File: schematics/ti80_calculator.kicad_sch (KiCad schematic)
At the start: 117 parts, among them J10 0, J13 0, J14 0Ω, J15 0Ω, J16 0, J17 0Ω, J18 0, J5 0Ω, J7 0Ω, J8 0, J9 0Ω, Q1 RIQ, Q2 LG, Q3 LG, SW1 Slide Switch, SW10 CLEAR, SW11 VARS, SW12 PRGM, SW13 FRAC, SW14 MATH, SW15 MODE, SW17 ^, SW18 TAN, SW19 COS, SW2 ON, SW20 SIN, SW21 x⁻¹, SW22 2nd, SW24 ÷, SW25 ), SW26 (, SW27 ,, SW28 x², SW29 Y=, SW30 ▲, SW31 ×, SW32 9, SW33 8, SW34 7, SW35 LOG, SW36 WINDOW, SW37 ◄, SW38 -, SW39 6, SW40 5, SW41 4, SW42 LN, SW43 ZOOM, SW44 ►, SW45 +, SW46 3, SW47 2, SW48 1, SW49 STO►, SW5 STAT, SW50 TRACE, SW51 ▼, SW52 ENTER, SW53 (-), SW54 •, SW55 0, SW57 GRAPH, SW6 X,T, SW7 ALPHA, SW8 DEL, U1 T6M53A, U2 LH5359, U3 SRM2264, U4 T6B79

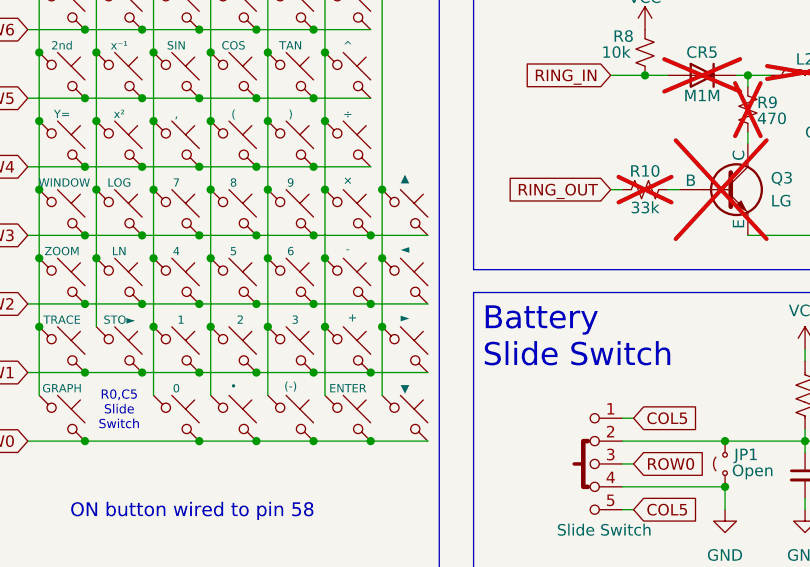
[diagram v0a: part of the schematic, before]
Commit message: Correct left/right arrow key rows to align with ti80doc
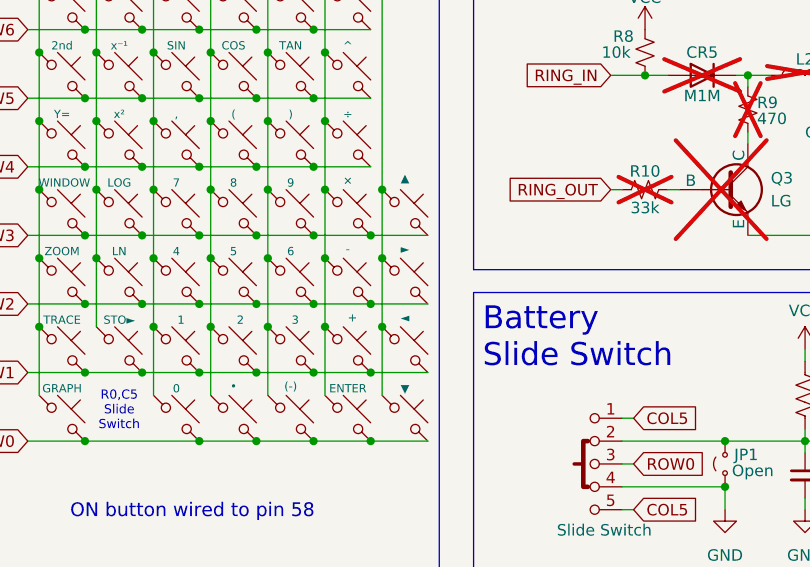
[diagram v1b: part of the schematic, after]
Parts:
- SW37: value ◄ -> ►
- SW44: value ► -> ◄
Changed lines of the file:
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@@
 			)
 		)
-		(property "Value" "►"
+		(property "Value" "◄"
 			(at 205.74 133.604 0)
 			(effects
@@
 			)
 		)
-		(property "Value" "◄"
+		(property "Value" "►"
 			(at 205.74 125.984 0)
 			(effects

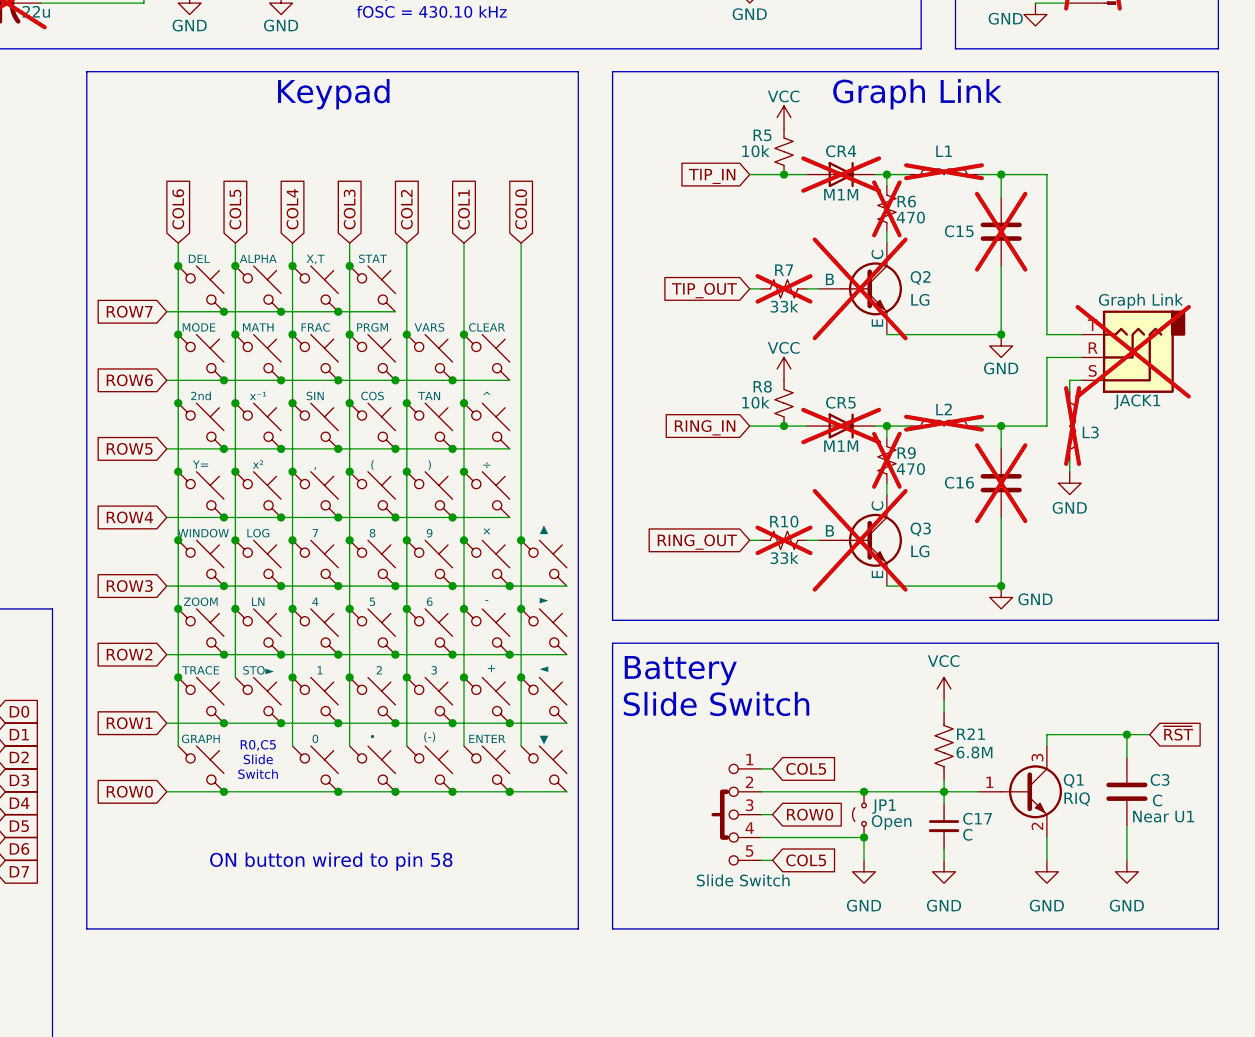
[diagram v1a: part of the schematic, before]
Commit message: Add custom TI-80 footprints and correct diode and transistor pins
- Correct diode and transistor pinouts to reflect the packages used
- Correct some labeling on the schematic
- Add custom footprints for graph link jack and ViewScreen
- Create some additional context layers in the PCB SVG
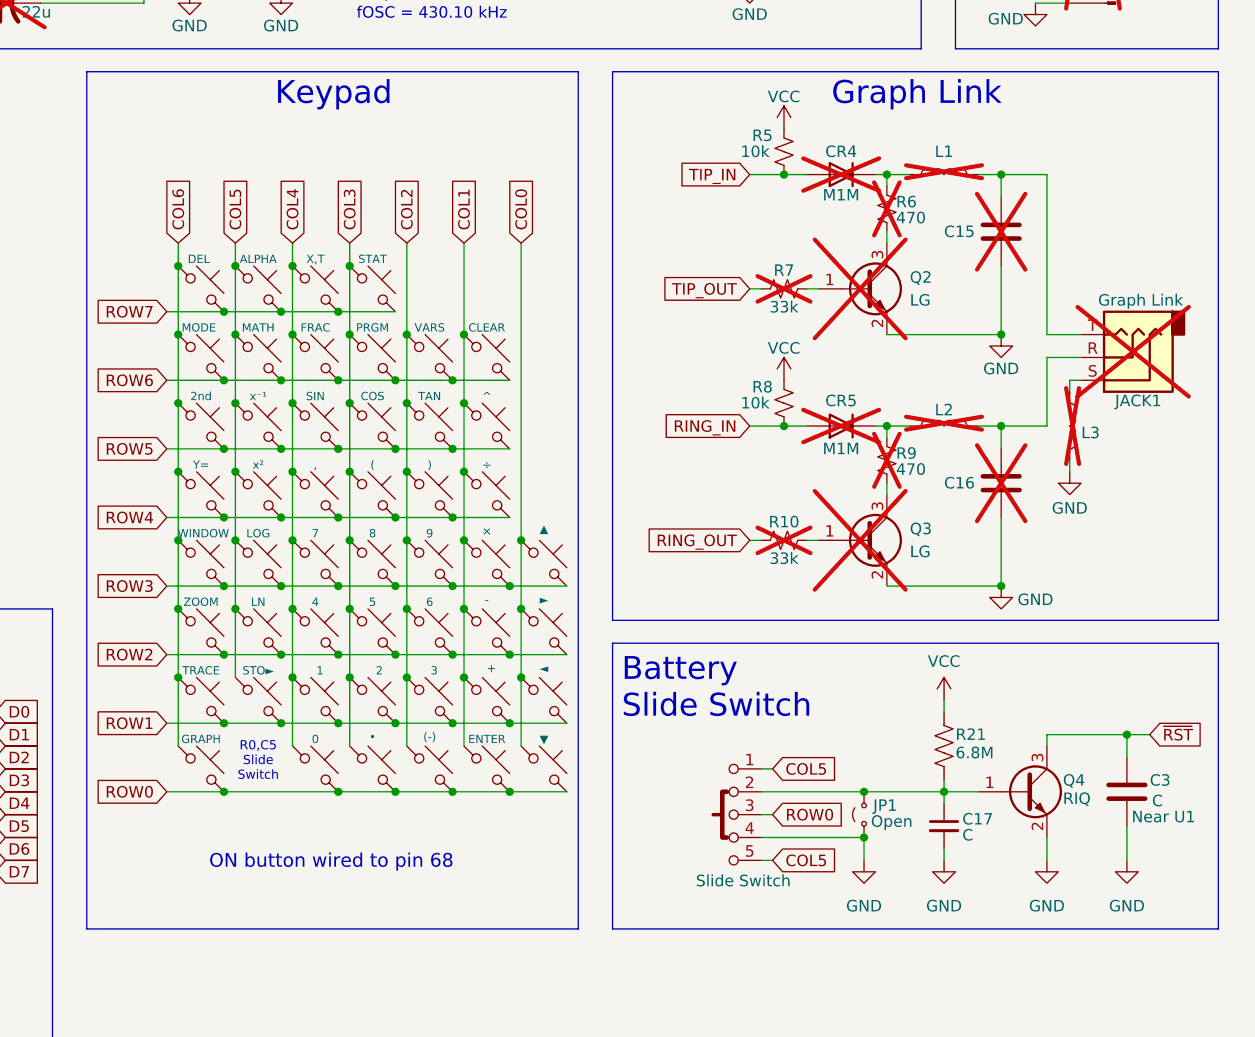
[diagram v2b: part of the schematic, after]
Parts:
- removed CR4, CR5: M1M, Package_TO_SOT_SMD:SOT-23, symbol Device:D
- removed Q2, Q3: LG, Package_TO_SOT_SMD:SOT-23, symbol Simulation_SPICE:NPN
- added CR4, CR5: M1M, Package_TO_SOT_SMD:SOT-23, symbol Diode:BAS19
- added Q2, Q3: LG, Package_TO_SOT_SMD:SOT-23-3, symbol Transistor_BJT:SS8050
- CR1, CR2: footprint Package_TO_SOT_SMD:SOT-23-5 -> ti80_footprint:Rohm_SC-74A-5_1.55x2.9mm_P0.95mm
- JACK1: footprint Connector_Audio:Jack_3.5mm_CUI_SJ-3523-SMT_Horizontal -> ti80_footprint:Graph_Link_Jack
- Q4: renamed from Q1; footprint Package_TO_SOT_SMD:SOT-23 -> Package_TO_SOT_SMD:SOT-323_SC-70_Handsoldering
- R4: footprint Resistor_SMD:R_0805_2012Metric -> Resistor_SMD:R_1206_3216Metric
- VIEW-CON1: footprint Connector_Samtec_MicroMate:Samtec_T1M-16-X-S-RA_1x16-1MP_P1.0mm_Terminal_Horizontal -> ti80_footprint:TI80_ViewScreen
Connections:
- net GND: now also Q2.2 (E), Q3.2 (E)
- net RING_IN: now also CR5.1 (A)
- net TIP_IN: now also CR4.1 (A)
- net at L2.2, R9.1: now also CR5.3 (K)
- net at L1.2, R6.1: now also CR4.3 (K)
- net at R6.2: now also Q2.3 (C)
- net at R7.2: now also Q2.1 (B)
- net at R9.2: now also Q3.3 (C)
- net at R10.2: now also Q3.1 (B)
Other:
- note added: "ON button wired to pin 68"
- note removed: "ON button wired to pin 58"

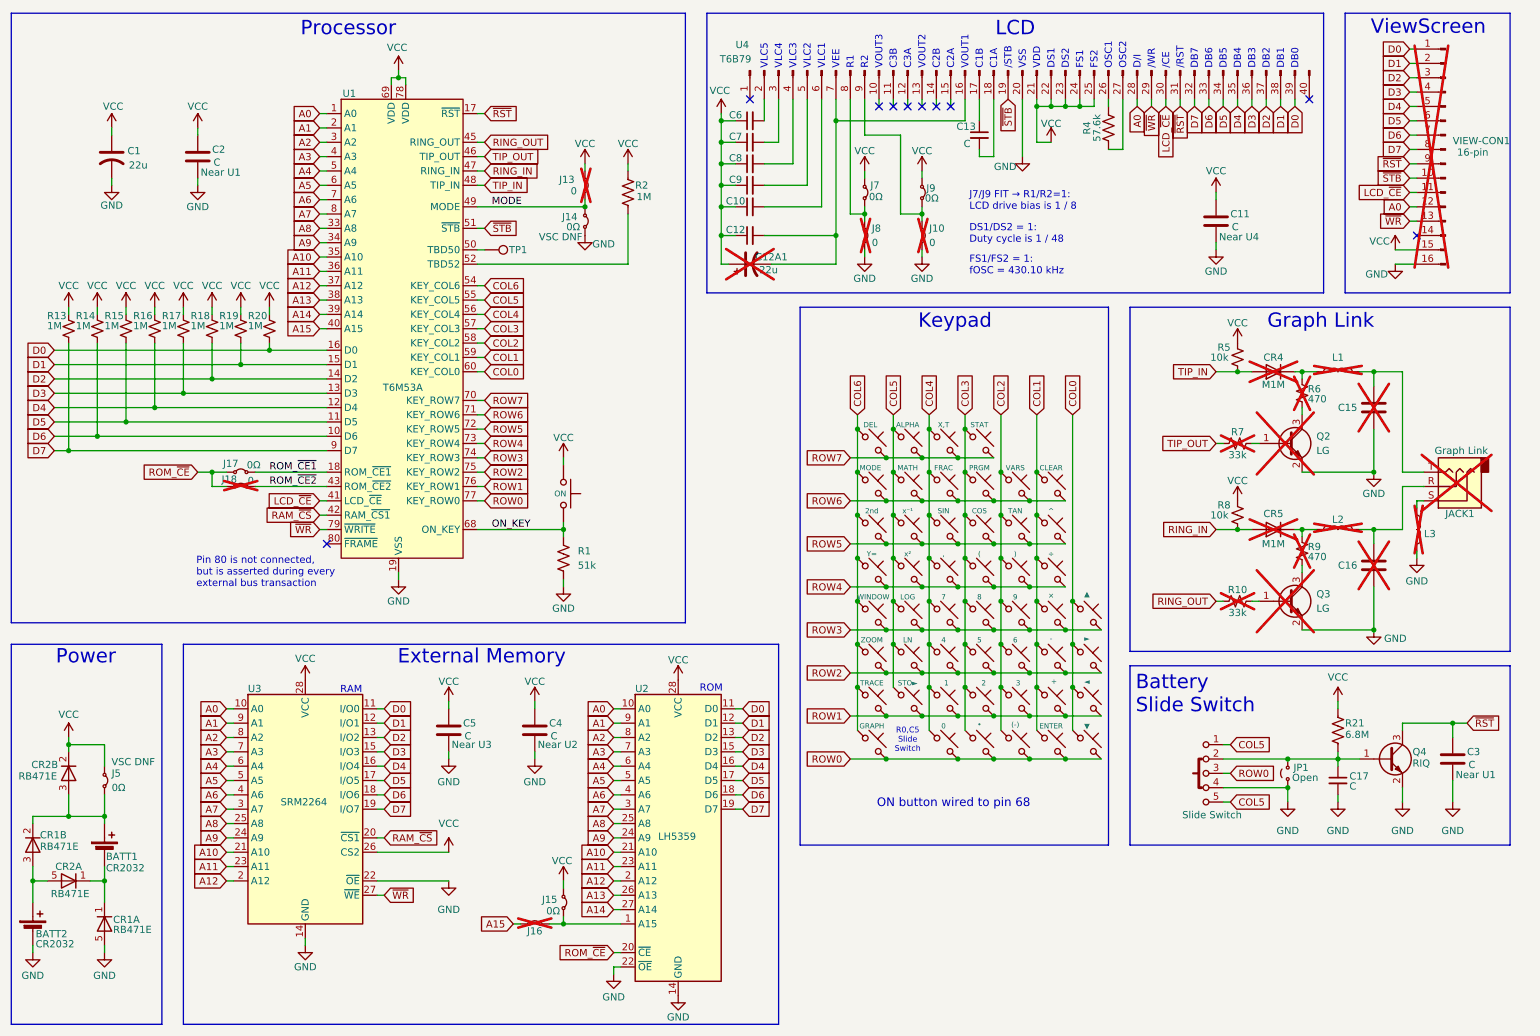
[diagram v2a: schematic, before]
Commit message: Add test points for power and keypad
- Add battery test points on front and back of PCB
- Add test points for row and columns on keypad side of PCB
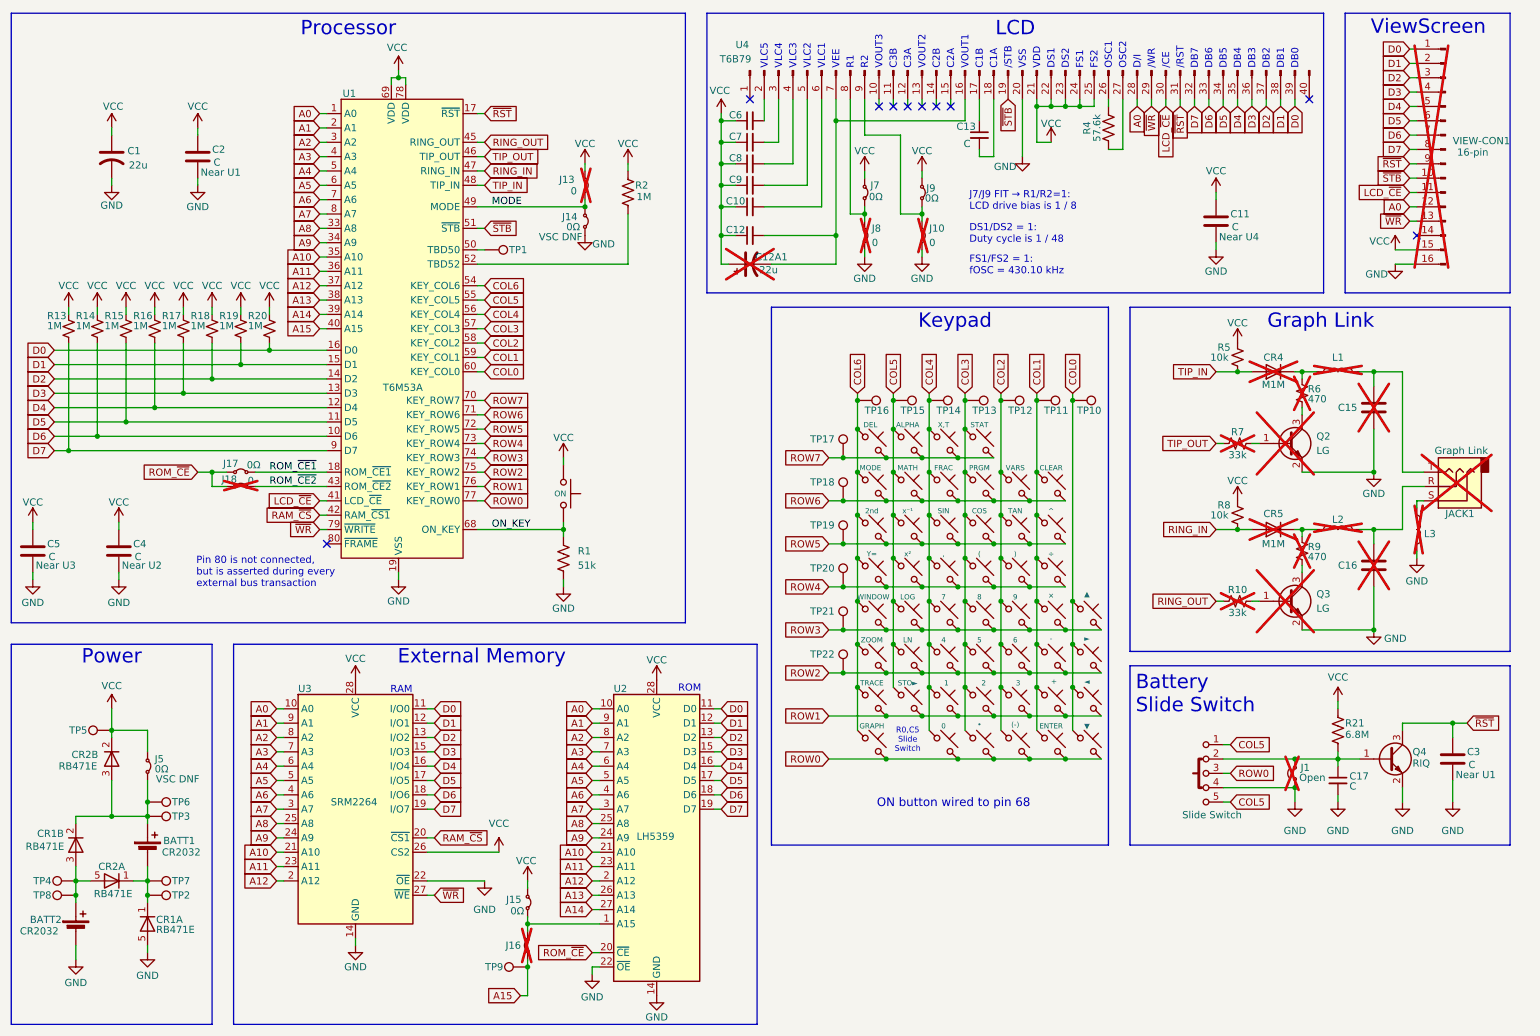
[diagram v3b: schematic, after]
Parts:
- added TP10, TP11, TP12, TP13, TP14, TP15, TP16, TP17, TP18, TP19, TP2, TP20, TP21, TP22, TP3, TP4, TP5, TP6, TP7, TP8, TP9: Pin 50 Test Point, TestPoint:TestPoint_Pad_D2.0mm, symbol Connector:TestPoint
- J1: renamed from JP1; footprint (none) -> Resistor_SMD:R_0805_2012Metric; now not fitted
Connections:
- net A15: now also TP9.1
- net COL0: now also TP10.1
- net COL1: now also TP11.1
- net COL2: now also TP12.1
- net COL3: now also TP13.1
- net COL4: now also TP14.1
- net COL5: now also TP15.1
- net COL6: now also TP16.1
- net ROW2: now also TP22.1
- net ROW3: now also TP21.1
- net ROW4: now also TP20.1
- net ROW5: now also TP19.1
- net ROW6: now also TP18.1
- net ROW7: now also TP17.1
- net VCC: now also TP5.1
- net at BATT1.1 (+), CR1.2, CR2.3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: now also TP3.1, TP6.1
- net at BATT1.2 (-), CR1.1, CR2.1: now also TP2.1, TP7.1
- net at BATT2.1 (+), CR1.3, CR2.5: now also TP4.1, TP8.1
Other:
- moved on the sheet: BATT1, BATT2, C4, C5, CR1A, CR1B, CR2A, CR2B, J15, J16, J5, U2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
